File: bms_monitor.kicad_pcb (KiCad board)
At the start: 2 copper layers, 115 x 65 mm, 238 parts, among them CN1 10nF, CN10 10nF, CN11 10nF, CN12 10nF, CN13 10nF, CN14 10nF, CN2 10nF, CN3 10nF, CN4 10nF, CN5 10nF, CN6 10nF, CN7 10nF, CN8 10nF, CN9 10nF, J1 Conn_01x02, J10 TEMP0, J11 TEMP1, J12 Conn_01x05, J13 Conn_ARM_JTAG_SWD_10, J2 Conn_01x02, J3 Conn_01x02, J4 Conn_01x02, J5 CELLS, J6 TEMP0, J7 TEMP1, J8 Conn_01x05, J9 CELLS, Q1 NSV1C201MZ4, Q2 NSV1C201MZ4, U1 STM32L432KBUx, U10 CD74HC4067SM, U11 MP4541, U12 SM91502ALA, U13 SM91502ALA, U14 SM91502ALA, U3 DSC61XX, U4 TFBS4652, U5 LTC6811-1, U6 CD74HC4067SM, U7 MP4541, U8 SM91502ALA, U9 LTC6811-1

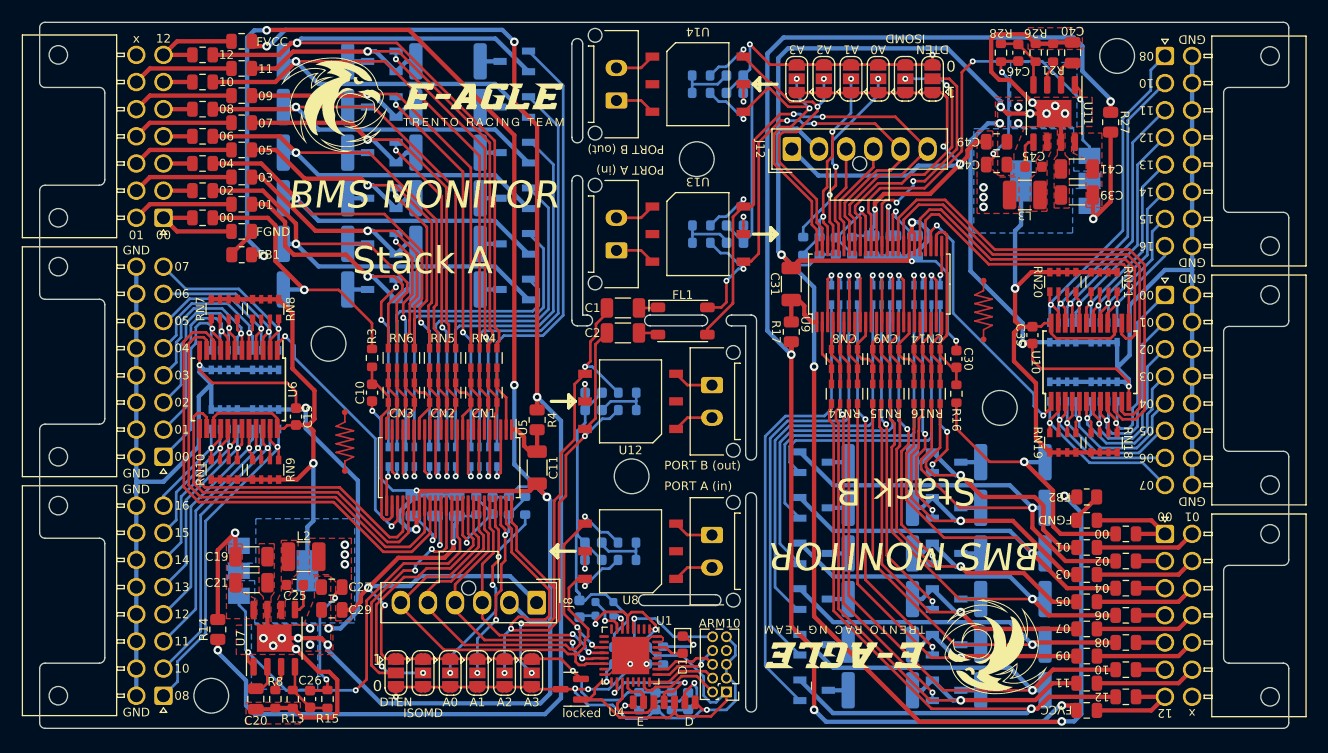
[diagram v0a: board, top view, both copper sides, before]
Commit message: pre production
- footprints change
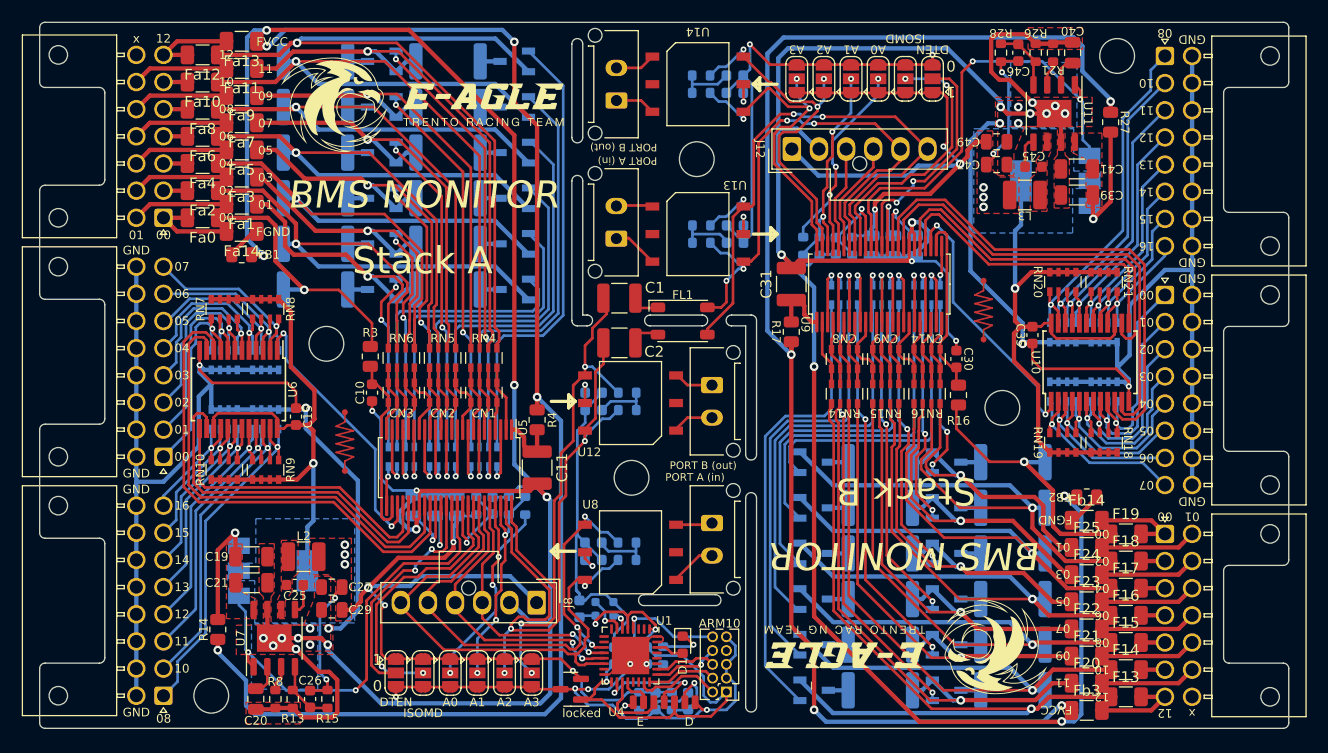
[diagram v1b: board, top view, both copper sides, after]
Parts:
- C1, C11, C2, C31: footprint Capacitor_SMD:C_1206_3216Metric -> Capacitor_SMD:C_1210_3225Metric
- F13, F14, F15, F16, F17, F18, F19, F20, F21, F22, F23, F24, F25, Fa0, Fa1, Fa10, Fa11, Fa12, Fa13, Fa14, Fa2, Fa3, Fa4, Fa5, Fa6, Fa7, Fa8, Fa9, Fb14, Fb3: footprint Fuse:Fuse_0805_2012Metric -> Fuse:Fuse_1206_3216Metric
- R16, R3: footprint Resistor_SMD:R_0603_1608Metric -> Resistor_SMD:R_0805_2012Metric
- moved J3 1.10 mm to (141.9, 108.1)
- moved J1 1.09 mm to (133.1, 81.9)
- moved C2 0.97 mm to (133.4, 91.5)
- moved C1 0.96 mm to (133.4, 87.4)
- moved H5 0.23 mm to (168.6, 97.5)
- moved R16 0.22 mm to (164.6, 96.3)
- moved R3 0.21 mm to (110.4, 92.8)
- moved H2 0.20 mm to (106.4, 91.6)
- moved U12 0.15 mm to (134.4, 97.1)
- moved H1 0.14 mm to (134.5, 103.9)
- moved U8 0.09 mm to (134.4, 110.8)
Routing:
- net /StackA/A3: track 52.2 -> 53.1 mm
- net /StackA/A2: track 57.8 -> 57.2 mm
- net /StackA/MUX_OUT: track 25.3 -> 25.8 mm

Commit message: pre production
footprint change
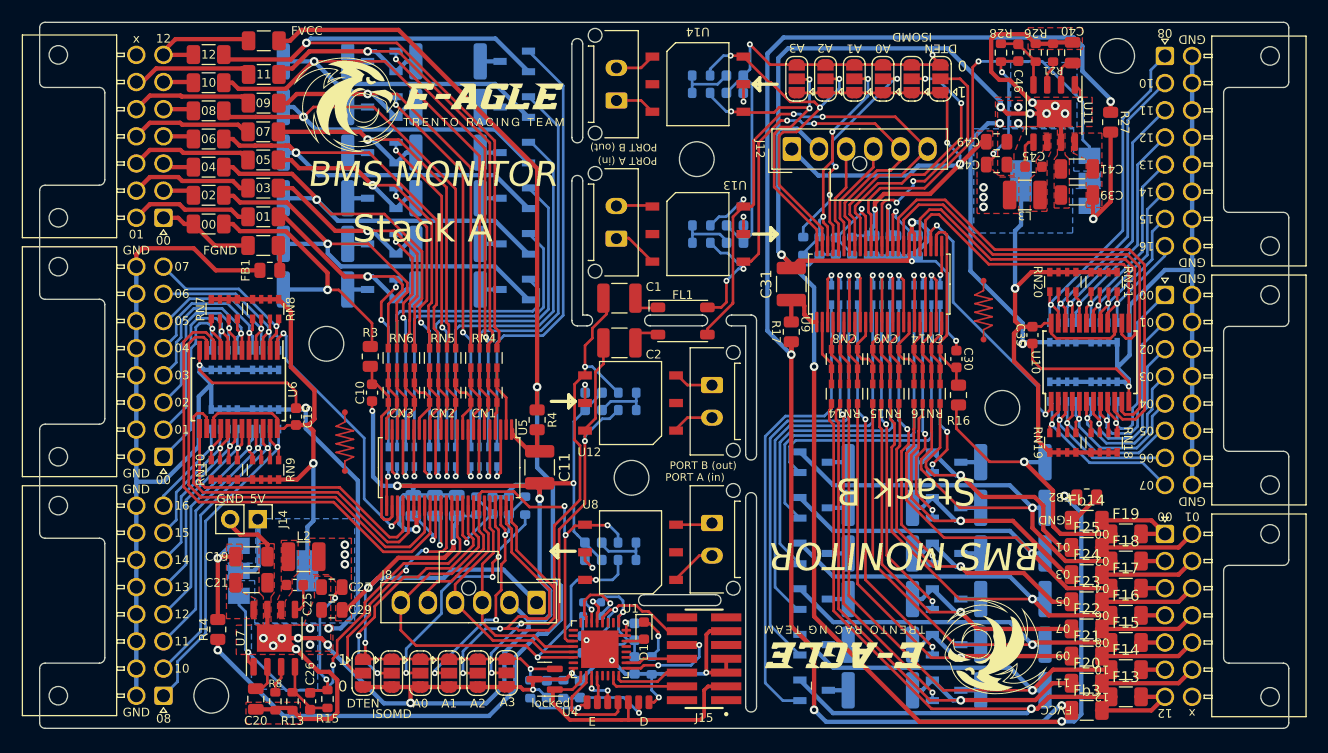
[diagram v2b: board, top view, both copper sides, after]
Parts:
- removed J13: Conn_ARM_JTAG_SWD_10, Connector_PinHeader_1.27mm:PinHeader_2x05_P1.27mm_Vertical
- added J14: 5V, Connector_PinHeader_2.54mm:PinHeader_1x02_P2.54mm_Vertical, F.Cu at (100.1, 107.7)
- added J15: Conn_ST_STDC14, lib:SAMTEC_FTSH-107-01-L-DV-K-TR, F.Cu at (141.2, 120.6)
- moved R1 10.1 mm to (125.2, 123.4)
- moved C9 10.1 mm to (126.7, 123.4)
- moved R2 10.0 mm to (128.2, 123.4)
- moved C8 10.0 mm to (129.7, 123.4)
- moved C7 5.49 mm to (134.8, 118.1)
- moved U4 4.25 mm to (133.2, 124.6)
- moved D1 3.79 mm to (135.6, 118.0)
- moved C5 3.08 mm to (130.0, 119.3)
- moved C4 3.05 mm to (131.5, 119.3)
- moved JP5 3.03 mm to (109.8, 121.9)
- moved FB1 2.96 mm to (101.2, 84.8), turned to 180 degrees
- moved JP6 2.89 mm to (112.4, 121.9)
- moved U1 2.89 mm to (131.6, 119.7)
- moved JP1 2.75 mm to (115.1, 121.9)
- moved JP2 2.61 mm to (117.7, 121.9)
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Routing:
- net GND: track 412.3 -> 322.5 mm
- net /StackA/VDD: track 127.1 -> 114.5 mm, vias 4 -> 2
- net /IA+_A: track 48.8 -> 40.9 mm
- net /StackA/A0: track 22.5 -> 27.8 mm
- net /StackA/A2: track 57.2 -> 61.9 mm
- net /StackA/CC01: track 30.3 -> 26.1 mm
- net +3.3V: track 46.7 -> 42.8 mm, vias 3 -> 2
- net /MOSI: track 27.0 -> 23.1 mm, vias 2 -> 0
- net /StackA/A1: track 20.9 -> 24.8 mm
- net /TDI: track 6.18 -> 9.84 mm, vias 1 -> 2
- net Net-(R1-Pad1): track 2.35 -> 5.82 mm
- net /StackA/CC05: track 36.8 -> 33.5 mm
- net +5V: track 142.4 -> 139.3 mm
- net /MISO: track 23.7 -> 20.6 mm, vias 2 -> 0
- net Net-(U1-Pad19): track 6.75 -> 3.81 mm, vias 0 -> 2
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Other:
- board text added: "RESET"
- board text added: "SWCLK"
- board text added: "SWDIO"
- board text added: "SWO"
- board text added: "TDI"
- board text removed: "ARM10"
- board text removed: "~{RESET} TDI SWO/TDO SWCLK/TCK SWDIO/TMS"

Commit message: production candidate
- footprint change
- added ltc6811-2 full compatibility
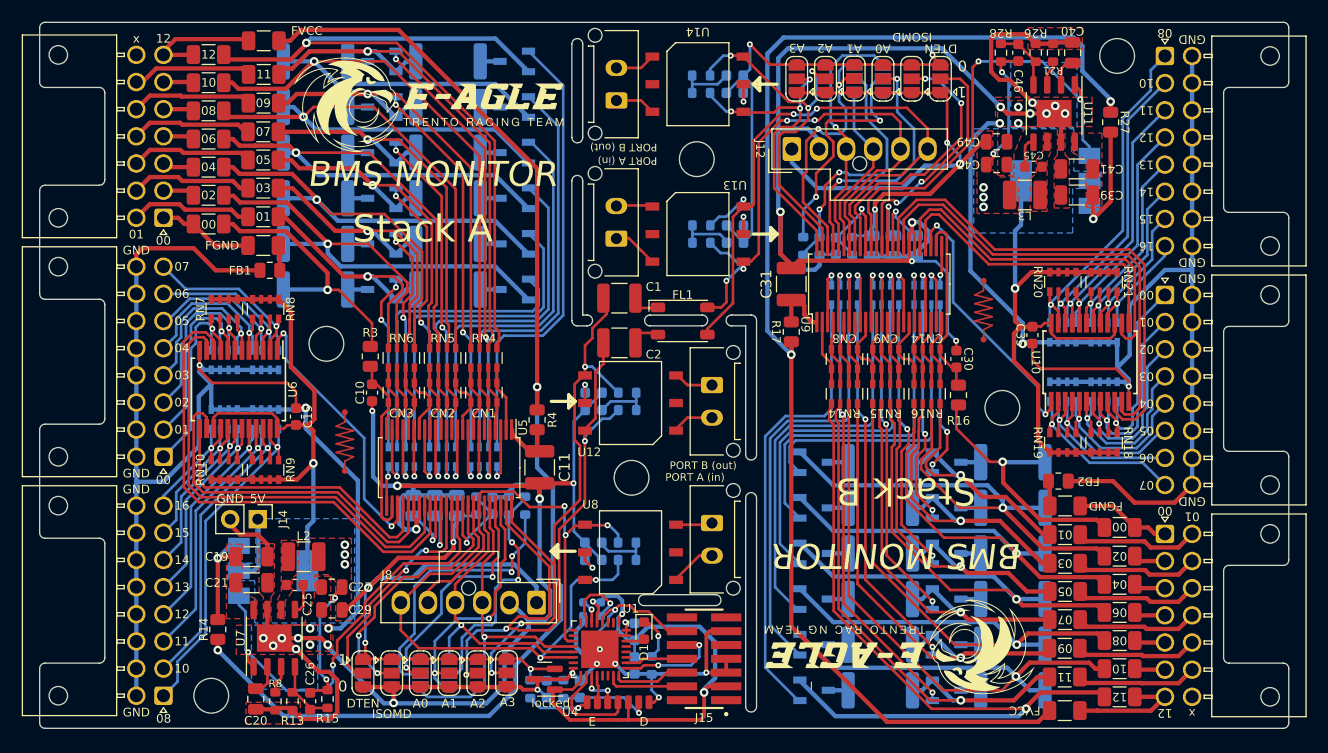
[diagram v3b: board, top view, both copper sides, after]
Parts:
- added JP13: IBIAS, Jumper:SolderJumper-3_P1.3mm_Open_RoundedPad1.0x1.5mm, B.Cu at (115.1, 121.9)
- added JP14: ICMP, Jumper:SolderJumper-3_P1.3mm_Open_RoundedPad1.0x1.5mm, B.Cu at (117.7, 121.9)
- added JP15: IBIAS, Jumper:SolderJumper-3_P1.3mm_Open_RoundedPad1.0x1.5mm, B.Cu at (157.6, 67.2)
- added JP16: ICMP, Jumper:SolderJumper-3_P1.3mm_Open_RoundedPad1.0x1.5mm, B.Cu at (155.0, 67.2)
- moved FB2 2.99 mm to (173.8, 104.2), turned to 0 degrees
- moved C5 2.59 mm to (132.6, 119.2), turned to -90 degrees
- moved Fb14 2.40 mm to (174.4, 106.5)
- moved F25 2.33 mm to (174.4, 109.2)
- moved F24 2.26 mm to (174.4, 111.8)
- moved F23 2.22 mm to (174.4, 114.4)
- moved F22 2.18 mm to (174.4, 117.0)
- moved F21 2.15 mm to (174.4, 119.6)
- moved F20 2.11 mm to (174.4, 122.3)
- moved Fb3 2.03 mm to (174.4, 125.4)
- moved C4 1.02 mm to (130.5, 119.3)
- moved F19 0.82 mm to (179.4, 108.5)
- moved F18 0.73 mm to (179.4, 111.2)
- moved F17 0.68 mm to (179.4, 113.7)
- moved F16 0.63 mm to (179.4, 116.3)
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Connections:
- net /StackB/SDO renamed /StackB/IBIAS_2
- R18 pad 1: /StackB/A1 -> Net-(R18-Pad1)
- R18 pad 2: /StackB/A0 -> Net-(R18-Pad2)
- R19 pad 2: /StackB/A1 -> Net-(R18-Pad1)
- R5 pad 1: /StackA/A1 -> Net-(R5-Pad1)
- R5 pad 2: /StackA/A0 -> Net-(R5-Pad2)
- R6 pad 2: /StackA/A1 -> Net-(R5-Pad1)
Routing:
- net /StackB/GND: track 353.1 -> 287.2 mm, vias 20 -> 17
- net Net-(R5-Pad2): track 0.00 -> 25.9 mm, vias 0 -> 2
- net Net-(R18-Pad1): track 0.00 -> 23.4 mm, vias 0 -> 2
- net Net-(R18-Pad2): track 0.00 -> 21.9 mm, vias 0 -> 2
- net Net-(R5-Pad1): track 0.00 -> 21.9 mm, vias 0 -> 2
- net /StackB/IBIAS_2: track 9.48 -> 23.2 mm, vias 0 -> 1
- net /MISO: track 20.6 -> 32.5 mm, vias 0 -> 1
- net +3.3V: track 42.8 -> 52.4 mm, vias 2 -> 3
- net /StackB/SDI: track 10.4 -> 16.3 mm
- net /StackB/VDD: track 126.5 -> 121.0 mm, vias 4 -> 2
- net /MOSI: track 23.1 -> 27.6 mm, vias 0 -> 1
- net /StackB/CC01: track 30.3 -> 26.1 mm
- net /StackA/A0: track 27.8 -> 24.0 mm, vias 3 -> 2
- net /StackB/CC05: track 36.8 -> 33.9 mm
- net /StackB/CC07: track 41.1 -> 38.3 mm
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
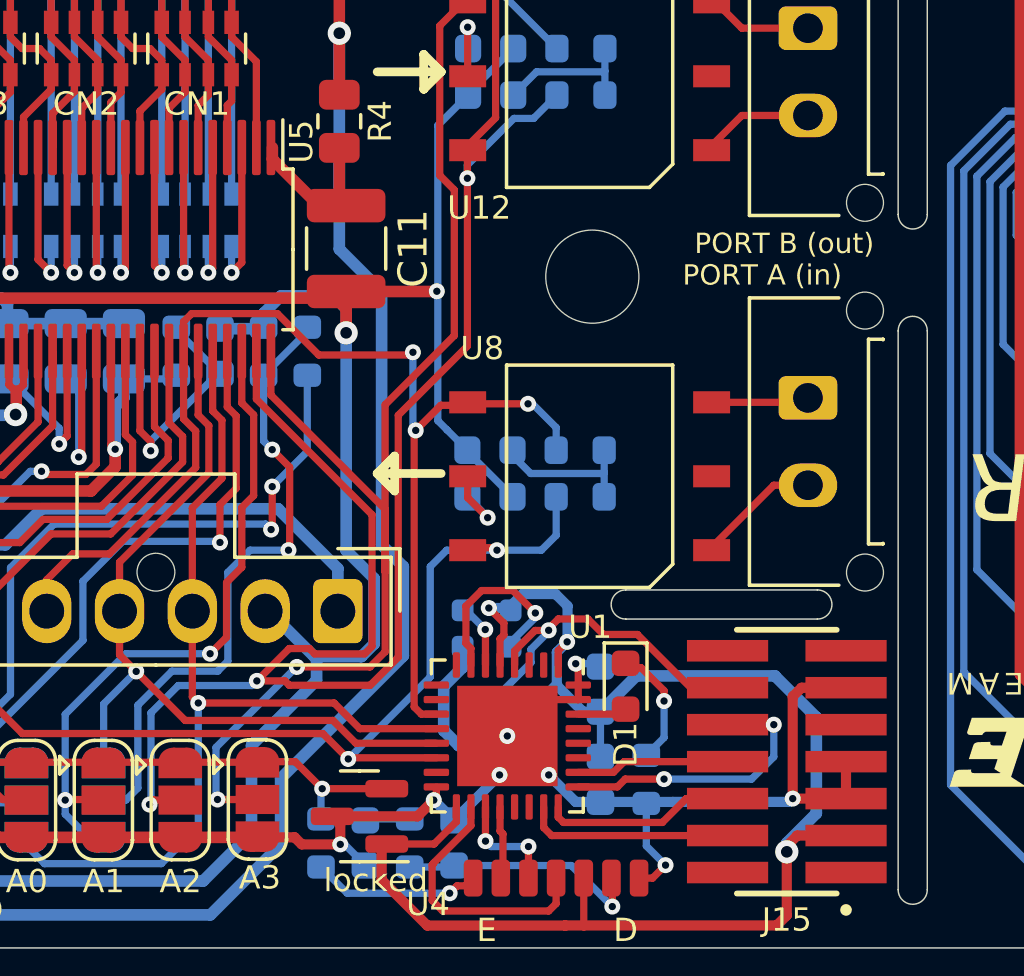
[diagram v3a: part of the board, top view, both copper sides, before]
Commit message: Addition
-Added USART 2 to Programming connector
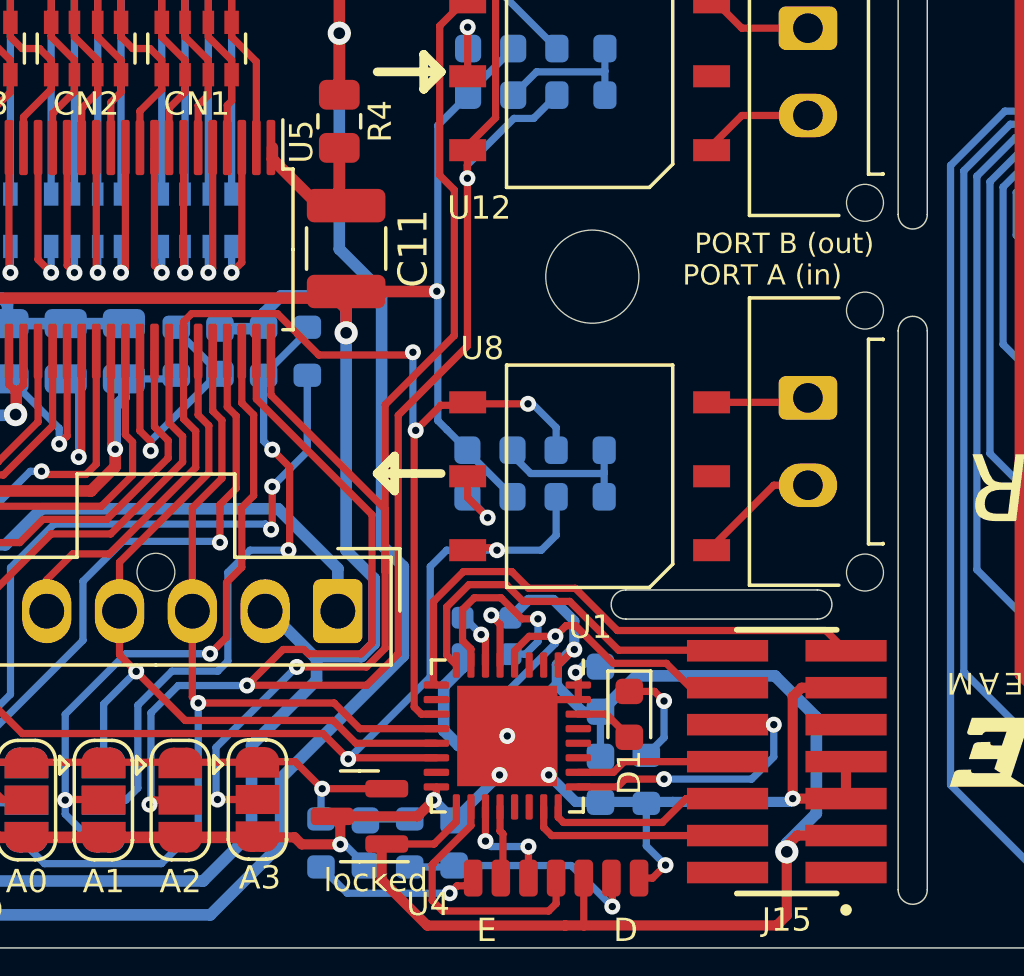
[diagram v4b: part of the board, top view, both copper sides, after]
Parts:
- moved D1 0.97 mm to (135.8, 119.0)
- moved U3 0.25 mm to (130.9, 116.3)
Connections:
- net /StackB/SDI renamed /StackB/ICMP_2
- J15 pad 13: unconnected-(J15-Pad13) -> /UART2_RX
- J15 pad 14: unconnected-(J15-Pad14) -> /UART2_TX
- U1 pad 8: unconnected-(U1-Pad8) -> /UART2_TX
- U1 pad 9: unconnected-(U1-Pad9) -> /UART2_RX
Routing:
- net /UART2_RX: track 0.00 -> 18.6 mm
- net /UART2_TX: track 0.00 -> 13.0 mm
- net Net-(U1-Pad7): track 6.38 -> 6.98 mm
- net Net-(D1-Pad1): track 3.97 -> 3.45 mm
